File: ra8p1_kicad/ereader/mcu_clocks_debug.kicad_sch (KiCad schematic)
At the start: 12 parts, among them J1 Cortex Debug 10-pin, SW1 RESET, SW2 BOOT, U1 R7KA8P1KFLCAC#UC0, Y1 24MHz

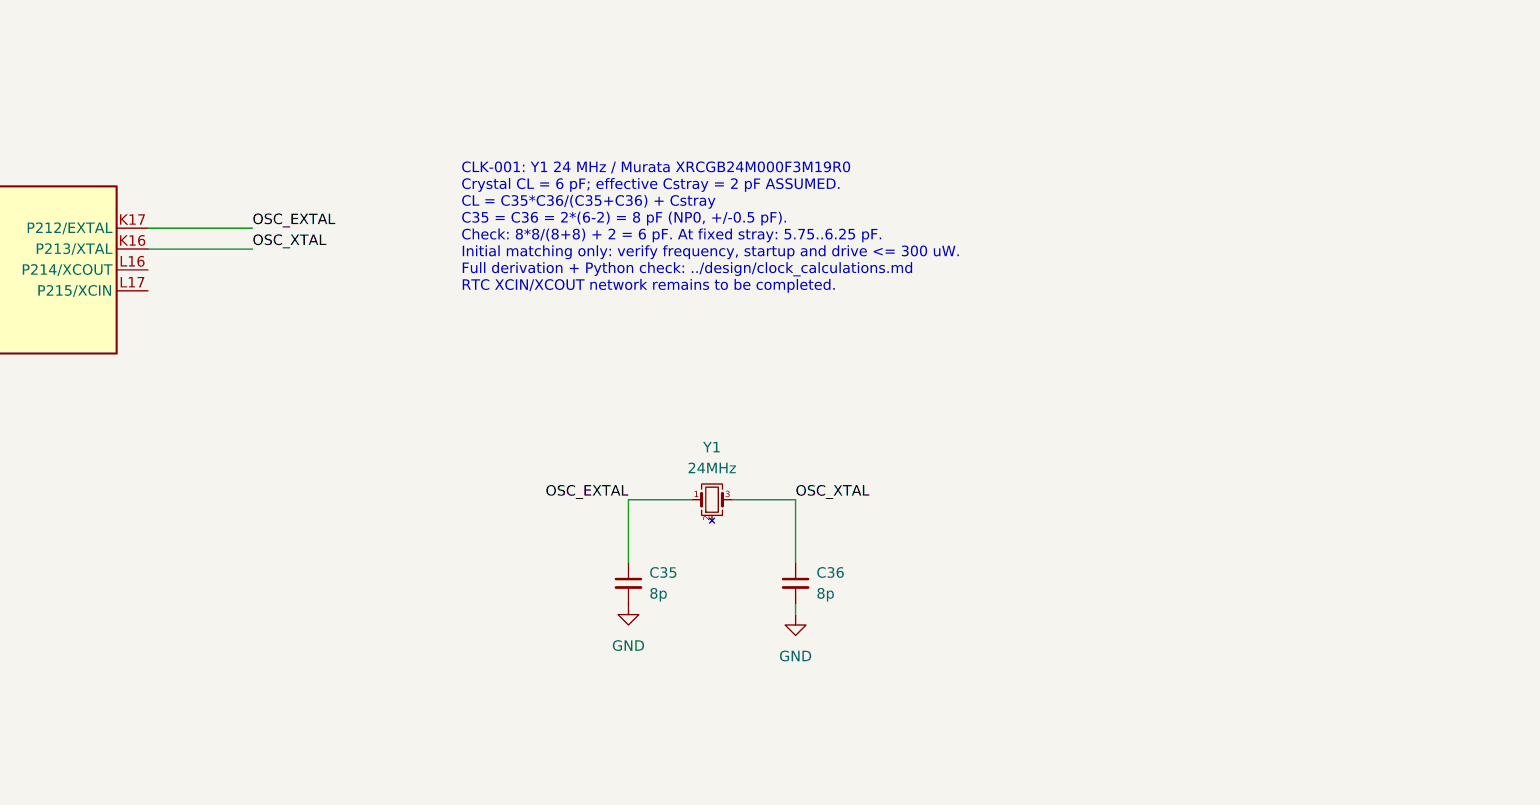
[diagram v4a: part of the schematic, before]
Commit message: feat(hardware): add RTC oscillator and verified load calculations
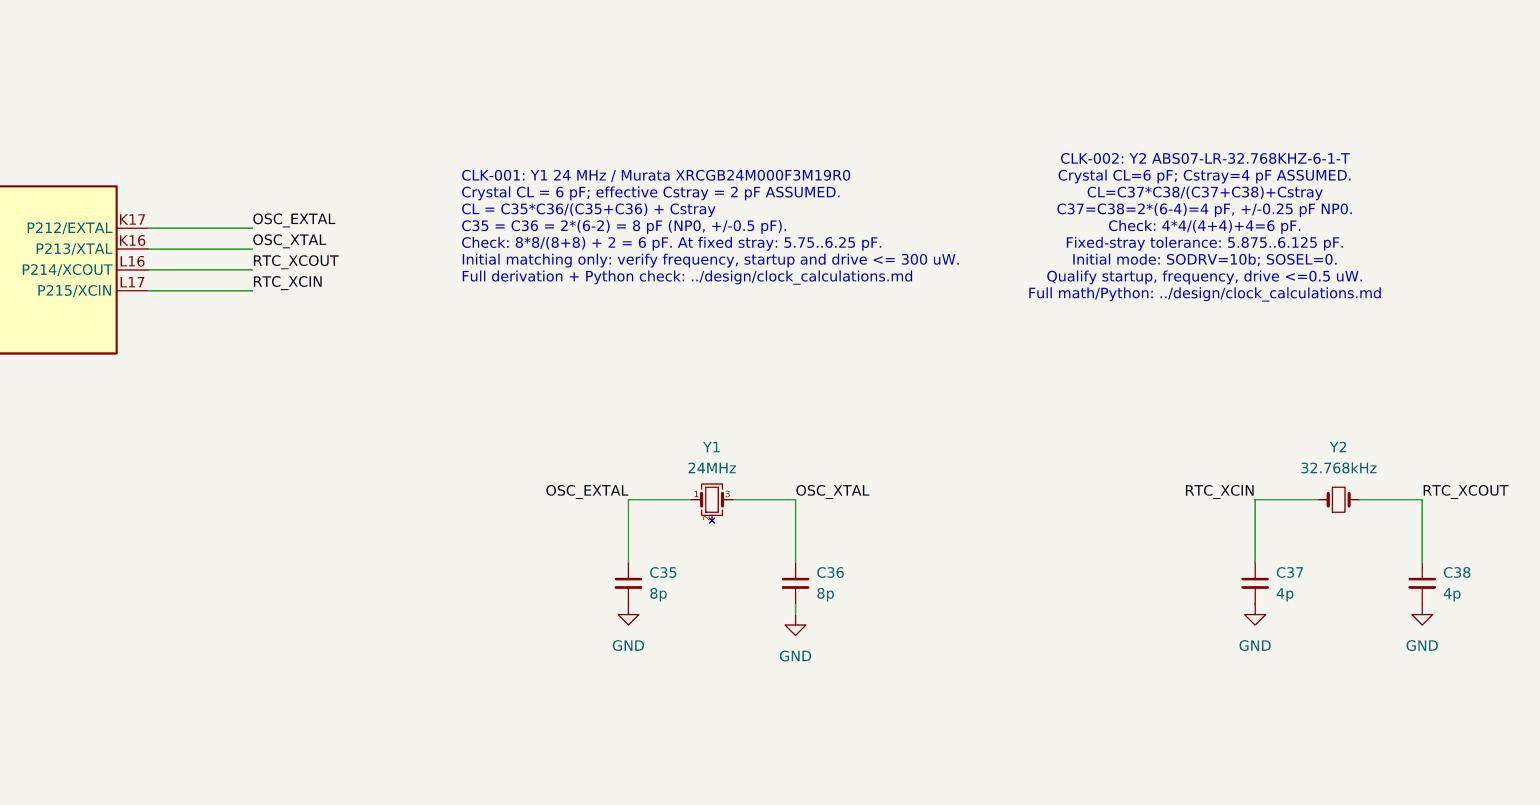
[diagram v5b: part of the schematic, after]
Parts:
- added C37, C38: 4p, symbol Device:C_Small
- added Y2: 32.768kHz, symbol Device:Crystal_Small
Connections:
- net GND: now also C37.2, C38.2
- net RTC_XCOUT: now reaches U1.L16 (P214/XCOUT)
- net RTC_XCOUT: now also C38.1, Y2.2
- net RTC_XCIN: now reaches U1.L17 (P215/XCIN)
- net RTC_XCIN: now also C37.1, Y2.1
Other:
- note added: "CLK-001: Y1 24 MHz / Murata XRCGB24M000F3M19R0 Crystal CL = 6 pF; effective Cstray = 2 pF ASSUMED. CL = C35*C36/(C35+C36) + Cstray C35 = C36 = 2*(6-2) = 8 pF (NP0, +/-0.5 pF). Check: 8*8/(8+8) + 2 = 6 pF. At fixed stray: 5.75..6.25 pF. Initial matching only: verify frequency, startup and drive <= 300 uW. Full derivation + Python check: ../design/clock_calculations.md"
- note added: "CLK-002: Y2 ABS07-LR-32.768KHZ-6-1-T Crystal CL=6 pF; Cstray=4 pF ASSUMED. CL=C37*C38/(C37+C38)+Cstray C37=C38=2*(6-4)=4 pF, +/-0.25 pF NP0. Check: 4*4/(4+4)+4=6 pF. Fixed-stray tolerance: 5.875..6.125 pF. Initial mode: SODRV=10b; SOSEL=0. Qualify startup, frequency, drive <=0.5 uW. Full math/Python: ../design/clock_calculations.md"
- note removed: "CLK-001: Y1 24 MHz / Murata XRCGB24M000F3M19R0 Crystal CL = 6 pF; effective Cstray = 2 pF ASSUMED. CL = C35*C36/(C35+C36) + Cstray C35 = C36 = 2*(6-2) = 8 pF (NP0, +/-0.5 pF). Check: 8*8/(8+8) + 2 = 6 pF. At fixed stray: 5.75..6.25 pF. Initial matching only: verify frequency, startup and drive <= 300 uW. Full derivation + Python check: ../design/clock_calculations.md RTC XCIN/XCOUT network remain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"
